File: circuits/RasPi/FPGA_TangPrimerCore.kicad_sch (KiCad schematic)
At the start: 0 parts

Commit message: ラズパイ基板とか
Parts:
- added C15, C16, C17, C18, C26: 0.1uF, Capacitor_SMD:C_0402_1005Metric, symbol Device:C
- added J5: Conn_01x05_Pin, Connector_PinHeader_2.54mm:PinHeader_1x05_P2.54mm_Vertical, symbol Connector:Conn_01x05_Pin
- added R29, R85, R86: 5.1k, Resistor_SMD:R_0402_1005Metri, symbol Device:R
- added U7: FPGA_TangPrimer25K_Core, MyLibrary:FPGA_TangPrimer25K_Core, symbol MyLibrary:FPGA_TangPrimer25K_Core
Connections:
- new net: R85.1, U7.B17 (E8_READY)
- new net: R86.1, U7.B25 (D7_DONE)
- new net +3.3V: C15.1, C16.1, C17.1, C18.1, C26.1
- new net +5V: U7.A52 (VDD_5V), U7.A54 (VDD_5V), U7.A56 (VDD_5V), U7.A58 (VDD_5V), U7.A60 (VDD_5V)
- new net 3.3V_TangPrimer: R85.2, R86.2, U7.A2 (VCCIO2/3), U7.A4 (VCCIO2/3), U7.A46 (VDD_3V3), U7.A48 (VDD_3V3), U7.A50 (VDD_3V3), U7.B24 (VCCIO0/1), U7.B26 (VCCIO0/1), U7.B29 (VCCIO6/7), U7.B31 (VCCIO6/7)
- new net GNDD: C15.2, C16.2, C17.2, C18.2, C26.2, J5.1 (Pin_1), R29.2, U7.A1 (GND), U7.A19 (GND), U7.A29 (GND), U7.A35 (GND), U7.A41 (GND), U7.A47 (GND), U7.A53 (GND), U7.A59 (GND), U7.B1 (GND), U7.B15 (GND), U7.B2 (GND), U7.B27 (GND), U7.B28 (GND), U7.B45 (GND), U7.B50 (GND), U7.B59 (GND), U7.B60 (GND)
- new net MIPI_CK_N: U7.A45 (M0_CK_N)
- new net MIPI_CK_P: U7.A43 (M0_CK_P)
- new net MIPI_D0_N: U7.A57 (M0_D0_N)
- new net MIPI_D0_P: U7.A55 (M0_D0_P)
- new net MIPI_D1_N: U7.A51 (M0_D1_N)
- new net MIPI_D1_P: U7.A49 (M0_D1_P)
- new net MIPI_D2_N: U7.A39 (M0_D2_N)
- new net MIPI_D2_P: U7.A37 (M0_D2_P)
- new net MIPI_D3_N: U7.A33 (M0_D3_N)
- new net MIPI_D3_P: U7.A31 (M0_D3_P)
- new net TCK: J5.2 (Pin_2), R29.1, U7.A21 (C1_TCK)
- new net TDI: J5.5 (Pin_5), U7.A27 (A3_TDI)
- new net TDO: J5.4 (Pin_4), U7.A25 (A2_TDO)
- new net TMS: J5.3 (Pin_3), U7.A23 (B1_TMS)
- new net nRECONFIG: U7.A13 (D8_RECONFIG)
- no-connect marks 0 -> 4
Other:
- added sheet RS485_Panel (RS485_Panel.kicad_sch)
- added sheet UI_TangPrimer (UI_TangPrimer.kicad_sch)
- note added: "リセット用ピンはRECONFIG? プルアップをつけるかどうか"

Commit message: PDFプロット
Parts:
- R29, R85, R86: footprint Resistor_SMD:R_0402_1005Metri -> Resistor_SMD:R_0402_1005Metric
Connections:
- net +3.3V is gone; now on net +5V: C15.1, C16.1, C17.1, C18.1, C26.1
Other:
- added sheet DAC (DAC.kicad_sch)
- sheet RS485_Panel ports: added FPGARX_Panel0TX, FPGARX_Panel1TX, FPGARX_Panel2TX, FPGARX_Panel3TX, FPGARX_Panel4TX, FPGARX_Panel5TX, FPGATX_Panel0RX, FPGATX_Panel1RX, FPGATX_Panel2RX, FPGATX_Panel3RX, FPGATX_Panel4RX, FPGATX_Panel5RX; removed Panel0, Panel1, Panel2, Panel3, Panel4, Panel5
- sheet UI_TangPrimer ports: added LED_B0, LED_B1, LED_B2, LED_B3; removed LED0, LED1, LED2, LED3
- note added: "パスコン"
- note added: "書き込み"
- moved on the sheet: C15, C16, C17, C18, J5, R29, R85, R86, U7

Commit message: シンボル・フットプリントMyLib->TomoshibiLib置き換え
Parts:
- U7: footprint MyLibrary:FPGA_TangPrimer25K_Core -> TomoshibiLibrary:FPGA_TangPrimer25K_Core; symbol MyLibrary:FPGA_TangPrimer25K_Core -> TomoshibiLibrary:FPGA_TangPrimer25K_Core
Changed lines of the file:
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@@
     )
   )
-  (symbol (lib_id "MyLibrary:FPGA_TangPrimer25K_Core") (at 111.76 91.44 0) (unit 1)
+  (symbol (lib_id "TomoshibiLibrary:FPGA_TangPrimer25K_Core") (at 111.76 91.44 0) (unit 1)
     (in_bom yes) (on_board yes) (dnp no)
     (property "Reference" "U7" (at 162.56 182.88 0)
@@
       (effects (font (size 1.27 1.27)))
     )
-    (property "Footprint" "MyLibrary:FPGA_TangPrimer25K_Core" (at 111.76 91.44 0)
+    (property "Footprint" "TomoshibiLibrary:FPGA_TangPrimer25K_Core" (at 76.2 30.48 0)
       (effects (font (size 1.27 1.27)) (justify bottom) hide)
     )
-    (property "Datasheet" "" (at 111.76 91.44 0)
+    (property "Datasheet" "" (at 88.9 30.48 90)
       (effects (font (size 1.27 1.27)) hide)
     )
-    (property "PARTREV" "2021-10-12" (at 111.76 91.44 0)
+    (property "PARTREV" "2021-10-12" (at 81.28 30.48 0)
       (effects (font (size 1.27 1.27)) (justify bottom) hide)
     )
-    (property "MANUFACTURER" "" (at 111.76 91.44 0)
+    (property "MANUFACTURER" "" (at 88.9 30.48 90)
       (effects (font (size 1.27 1.27)) (justify bottom) hide)
     )
-    (property "MAXIMUM_PACKAGE_HEIGHT" "5.188 mm" (at 111.76 91.44 0)
+    (property "MAXIMUM_PACKAGE_HEIGHT" "5.188 mm" (at 78.74 30.48 0)
       (effects (font (size 1.27 1.27)) (justify bottom) hide)
     )
-    (property "STANDARD" "Manufacturer Recommendations" (at 111.76 91.44 0)
+    (property "STANDARD" "Manufacturer Recommendations" (at 76.2 30.48 0)
       (effects (font (size 1.27 1.27)) (justify bottom) hide)
     )

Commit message: 更新
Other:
- note removed: "リセット用ピンはRECONFIG? プルアップをつけるかどうか"
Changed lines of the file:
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@@
     (stroke (width 0) (type default))
-  )
-  (text "リセット用ピンはRECONFIG?\nプルアップをつけるかどうか" (at 147.32 33.02 0)
-    (effects (font (size 5.56 5.56)) (justify left bottom))
   )
   (text "パスコン" (at 17.78 109.22 0)

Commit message: raspi基板回路図
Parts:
- removed C16, C17, C18, C26: 0.1uF, Capacitor_SMD:C_0402_1005Metric, symbol Device:C
- C15: value 0.1uF -> 1uF
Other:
- sheet RS485_Panel ports: added Panel_PWRCtrl; removed none

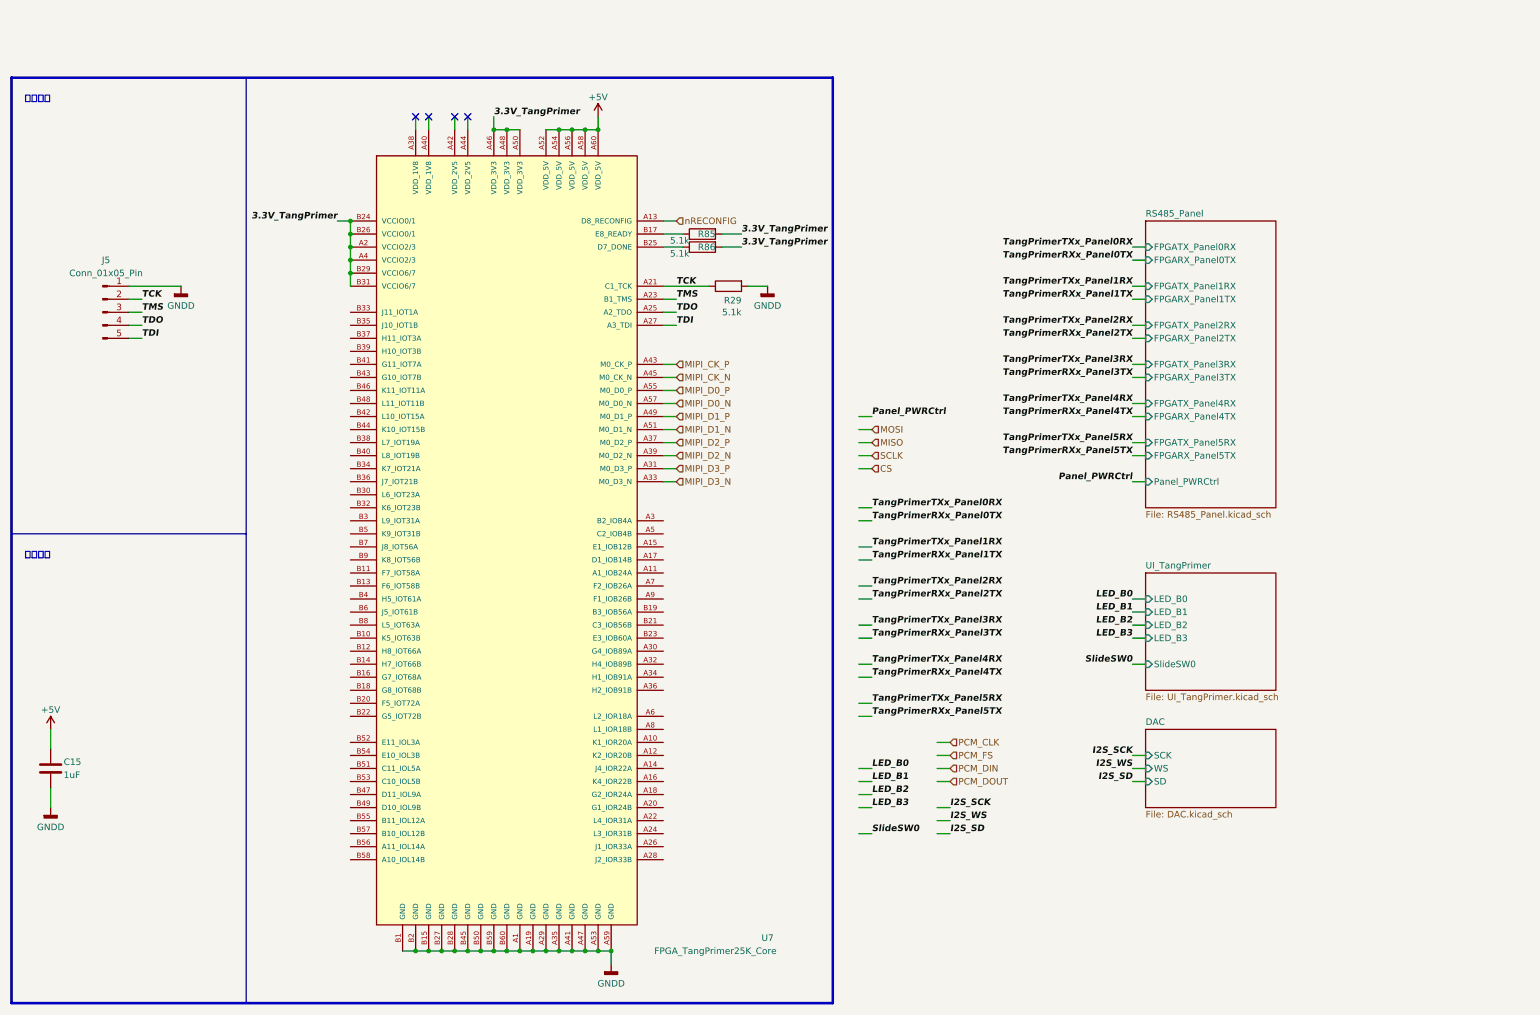
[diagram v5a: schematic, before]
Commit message: 発注第2弾
RasPi発注
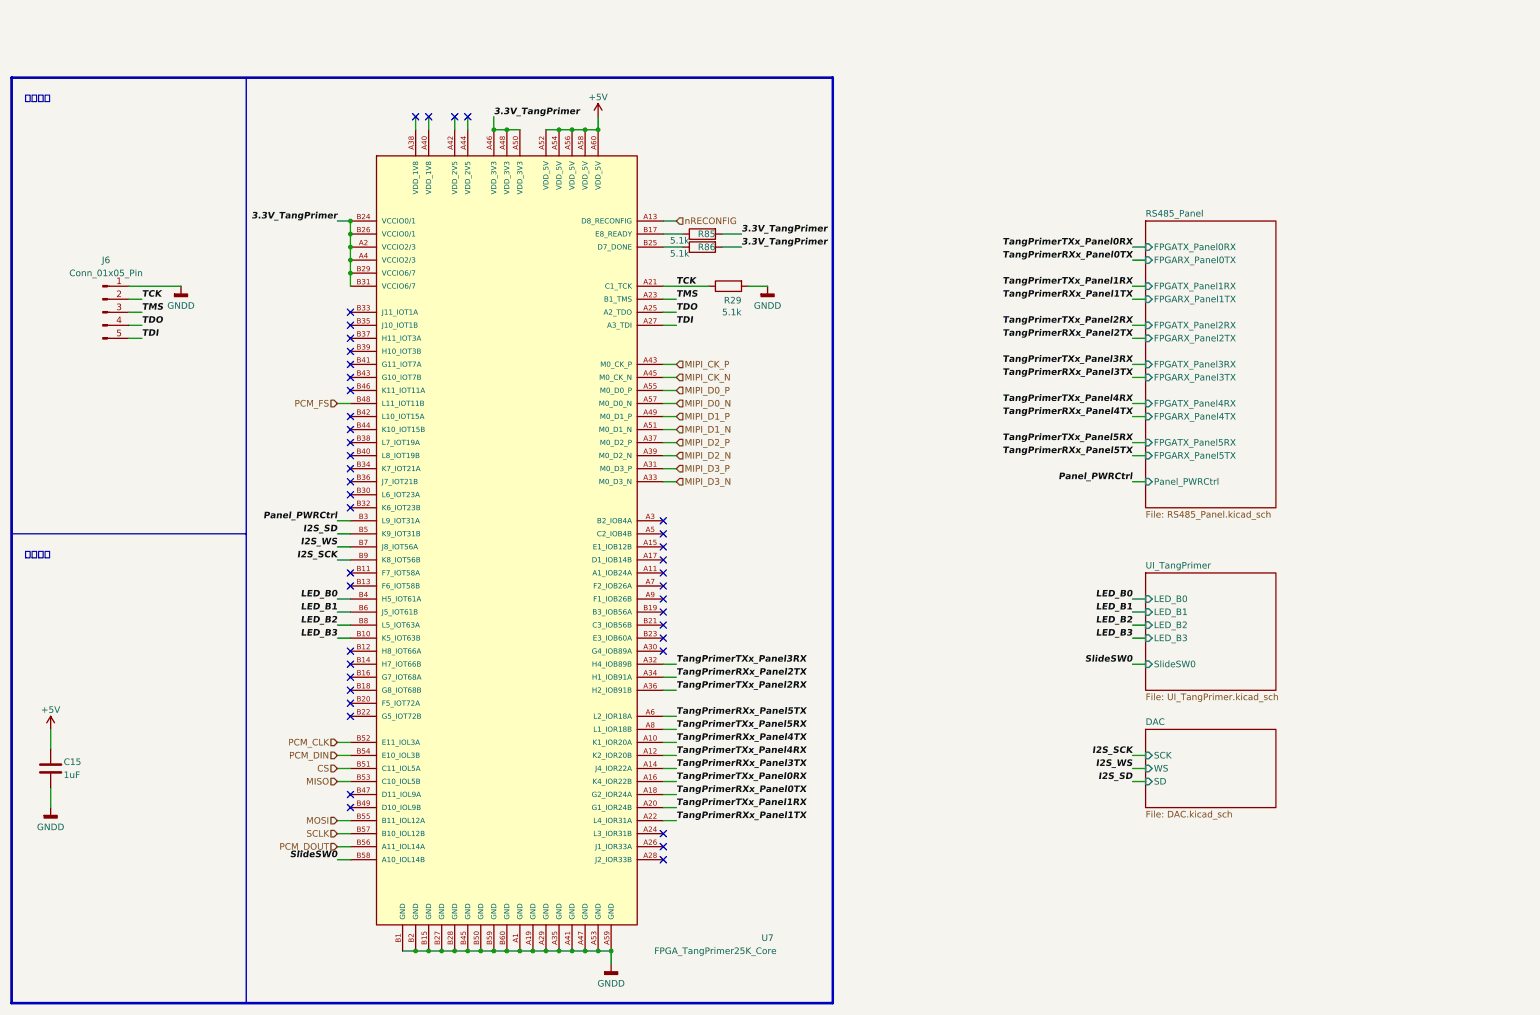
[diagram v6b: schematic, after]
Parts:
- renumbered J5 to J6
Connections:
- net CS: now also U7.B51 (C11_IOL5A)
- net I2S_SCK: now also U7.B9 (K8_IOT56B)
- net I2S_SD: now also U7.B5 (K9_IOT31B)
- net I2S_WS: now also U7.B7 (J8_IOT56A)
- net LED_B0: now also U7.B4 (H5_IOT61A)
- net LED_B1: now also U7.B6 (J5_IOT61B)
- net LED_B2: now also U7.B8 (L5_IOT63A)
- net LED_B3: now also U7.B10 (K5_IOT63B)
- net MISO: now also U7.B53 (C10_IOL5B)
- net MOSI: now also U7.B55 (B11_IOL12A)
- net PCM_CLK: now also U7.B52 (E11_IOL3A)
- net PCM_DIN: now also U7.B54 (E10_IOL3B)
- net PCM_DOUT: now also U7.B56 (A11_IOL14A)
- net PCM_FS: now also U7.B48 (L11_IOT11B)
- net Panel_PWRCtrl: now also U7.B3 (L9_IOT31A)
- net SCLK: now also U7.B57 (B10_IOL12B)
- net SlideSW0: now also U7.B58 (A10_IOL14B)
- net TangPrimerRXx_Panel0TX: now also U7.A18 (G2_IOR24A)
- net TangPrimerRXx_Panel1TX: now also U7.A22 (L4_IOR31A)
- net TangPrimerRXx_Panel2TX: now also U7.A34 (H1_IOB91A)
- net TangPrimerRXx_Panel3TX: now also U7.A14 (J4_IOR22A)
- net TangPrimerRXx_Panel4TX: now also U7.A10 (K1_IOR20A)
- net TangPrimerRXx_Panel5TX: now also U7.A6 (L2_IOR18A)
- net TangPrimerTXx_Panel0RX: now also U7.A16 (K4_IOR22B)
- net TangPrimerTXx_Panel1RX: now also U7.A20 (G1_IOR24B)
- net TangPrimerTXx_Panel2RX: now also U7.A36 (H2_IOB91B)
- net TangPrimerTXx_Panel3RX: now also U7.A32 (H4_IOB89B)
- net TangPrimerTXx_Panel4RX: now also U7.A12 (K2_IOR20B)
- net TangPrimerTXx_Panel5RX: now also U7.A8 (L1_IOR18B)
- no-connect marks 4 -> 43
